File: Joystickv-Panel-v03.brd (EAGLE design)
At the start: 100 x 48.9 mm, 58 parts, among them J1 AVR_SPI_PRG_6PTH, U1 JOYSTICKPTH, U3 V_REG_MIC5219SMD, U4 MCP73831

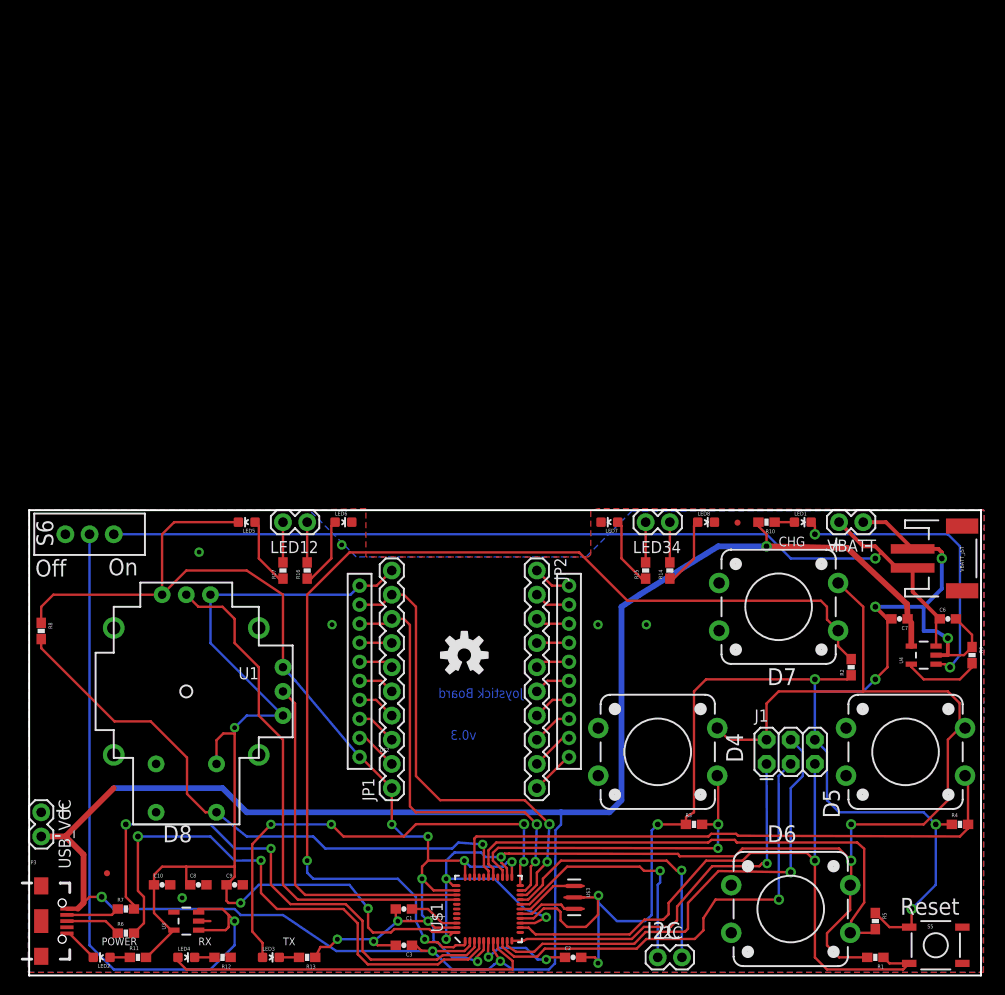
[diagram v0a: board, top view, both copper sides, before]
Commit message: Panel
Finished design, Panelized, and CAMed
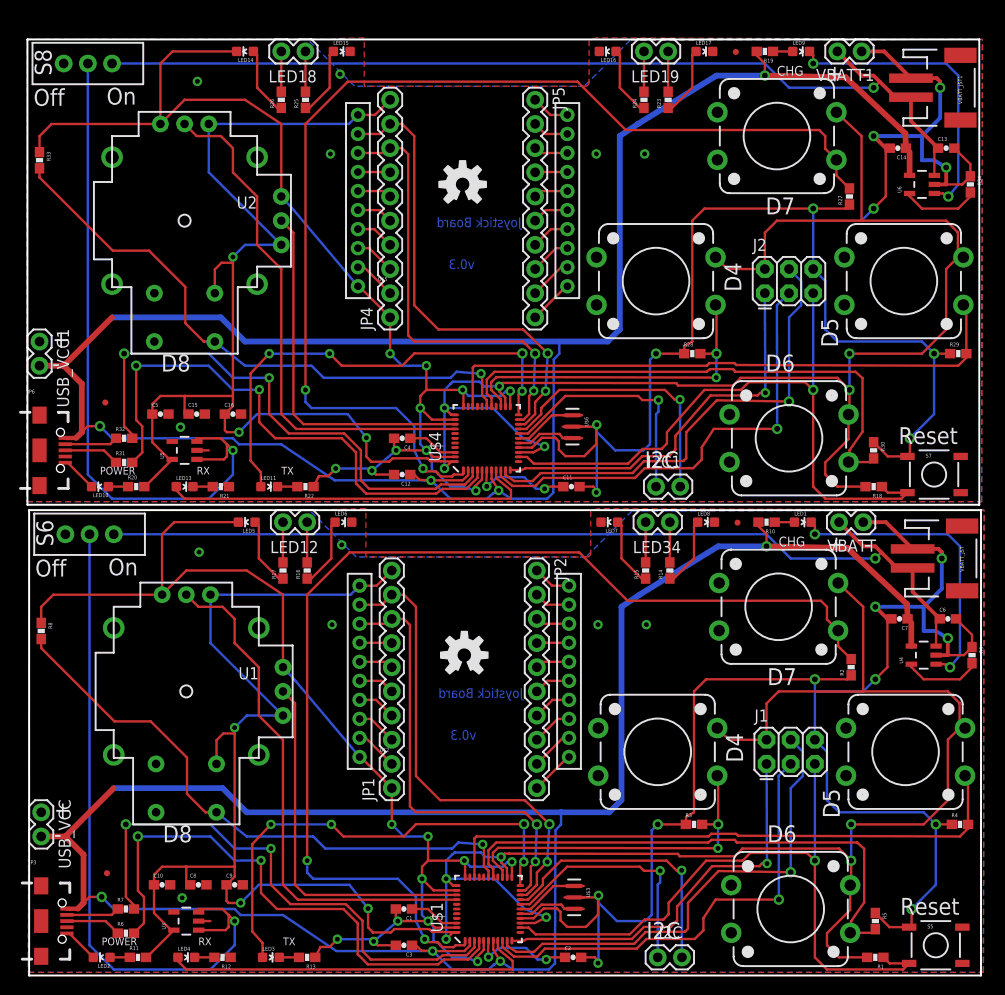
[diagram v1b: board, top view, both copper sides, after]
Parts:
- added C11, C12, C16: 1.0uF, SparkFun-Capacitors:0603-CAP
- added C13, C15: 10uF, SparkFun-Capacitors:0603-CAP
- added C14: 4.7uF, SparkFun-Capacitors:0603-CAP
- added C4, C5: 0.1uF, SparkFun-Capacitors:0603-CAP
- added FID3, FID4: FIDUCIALUFIDUCIAL, SparkFun-Aesthetics:MICRO-FIDUCIAL
- added I2C1, LED18, LED19, USB_VCC1, VBATT1: (no value), SparkFun-Connectors:1X02
- added J2: AVR_SPI_PRG_6PTH, SparkFun-Connectors:2X3
- added JP4, JP5: M10", SparkFun-Connectors:1X10
- added JP6: USB_MICROB_PLUGCONN-11752, SparkFun-Connectors:USB-B-MICRO-SMD_V03
- added LED10, LED16: RED, SparkFun-LED:LED-0603
- added LED11: Green, SparkFun-LED:LED-0603
- added LED13, LED15, LED9: Yellow, SparkFun-LED:LED-0603
- added LED14: GREEN, SparkFun-LED:LED-0603
- added LED17: BLUE, SparkFun-LED:LED-0603
- added LOGO2: OSHW-LOGOM, SparkFun-Aesthetics:OSHW-LOGO-M
- added R18, R27, R28, R29, R30, R33: 10K, SparkFun-Resistors:0603-RES
- added R19, R20: 470, SparkFun-Resistors:0603-RES
- added R21, R22, R23, R24, R25, R26: 330, SparkFun-Resistors:0603-RES
- added R31, R32: 22, SparkFun-Resistors:0603-RES
- added R34: 2.0k, SparkFun-Resistors:0603-RES
- added S10, S11, S12, S9: SWITCH-MOMENTARY-212MM, SparkFun-Electromechanical:TACTILE-PTH-12MM
- added S7: Reset, SparkFun-Electromechanical:TACTILE-SWITCH-SMD
- added S8: (no value), SparkFun-Electromechanical:SWITCH-SPDT
- added U$4: ATMEGA32U41:1-LESS_PASTE, SparkFun-DigitalIC:QFN-44-NOPAD_1:1-LESS_PASTE
- added U$5: XBEE-1B1, SparkFun-RF:XBEE-1
- added U$6: 8MHZ, SparkFun-FreqCtrl:RESONATOR-SMD
- added U2: JOYSTICKPTH, SparkFun-Electromechanical:JOYSTICK
- added U5: V_REG_MIC5219SMD, SparkFun-PowerIC:SOT23-5
- added U6: MCP73831, SparkFun-PowerIC:SOT23-5
- added VBATT_JST1: (no value), SparkFun-Connectors:JST-2-SMD
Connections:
- new net 3.3V1: C15.1, C16.1, C5.1, J2.2, JP4.10, R18.2, R20.2, S10.3, S11.3, S12.3, S9.3, U$4.14, U$4.24, U$4.34, U$4.44, U$5.1, U2.B2A, U2.H1, U2.V1, U5.5
- new net A2: U$4.36, U2.V2
- new net A3: U$4.37, U2.H2
- new net D+1: R31.2, U$4.4
- new net D-1: R32.2, U$4.3
- new net D1: I2C1.2, U$4.18
- new net D11: R28.2, S10.1, U$4.25
- new net D12: R29.2, S11.1, U$4.31
- new net D13: R30.2, S12.1, U$4.27
- new net D14: I2C1.1, U$4.19
- new net D15: R27.2, S9.1, U$4.1
- new net D16: R33.2, U$4.28, U2.B1A
- new net D17: U$4.29
- new net D18: U$4.30
- new net GND1: C11.2, C12.2, C13.2, C14.2, C15.2, C16.2, C4.2, C5.2, J2.6, JP4.1, JP6.GND1, LED10.C, LED14.C, LED15.C, LED16.C, LED17.C, R21.1, R22.1, R27.1, R28.1, R29.1, R30.1, R33.1, R34.1, S7.1, U$4.15, U$4.23, U$4.33, U$4.35, U$4.43, U$4.5, U$5.10, U$6.2, U2.H3, U2.V3, U5.2, U6.2, USB_VCC1.1, VBATT1.1, VBATT_JST1.1
- new net MISO1: J2.1, U$4.11
- new net MOSI1: J2.4, U$4.10
- new net N$22: C11.1, U$4.6
- new net N$41: R34.2, U6.5
- new net N$42: JP4.2, U$5.9
- new net N$43: JP4.3, U$5.8
- new net N$44: JP4.4, U$5.7
- new net N$45: JP4.5, U$5.6
- new net N$46: JP4.6, U$5.5
- new net N$47: JP4.7, U$5.4
- new net N$48: JP5.10, U$5.11
- new net N$49: JP5.9, U$5.12
- new net N$50: JP5.8, U$5.13
- new net N$51: JP5.7, U$5.14
- new net N$52: JP5.6, U$5.15
- new net N$53: JP5.5, U$5.16
- new net N$54: JP5.4, U$5.17
- new net N$55: JP5.3, U$5.18
- new net N$56: JP5.2, U$5.19
- new net N$57: JP5.1, U$5.20
- new net N$58: LED9.A, R19.1
- new net N$59: LED9.C, U6.1
- new net N$60: LED10.A, R20.1
- new net N$61: LED13.A, U$4.8
- new net N$62: LED13.C, R21.2
- new net N$63: LED11.C, R22.2
- new net N$64: LED11.A, U$4.22
- new net N$65: LED15.A, R25.1
- new net N$66: LED14.A, R26.1
- new net N$67: LED18.1, R26.2
- new net N$68: LED18.2, R25.2
- new net N$69: LED19.1, R24.2
- new net N$7: C4.1, U$4.42
- new net N$70: LED19.2, R23.2
- new net N$71: LED17.A, R23.1
- new net N$72: LED16.A, R24.1
- new net N$73: JP6.D+1, R31.1
- new net N$74: JP6.D-1, R32.1
- new net N$75: U$4.17, U$6.1
- new net N$76: U$4.16, U$6.3
- new net RESET1: J2.5, R18.1, S7.3, U$4.13
- new net RX1: JP4.9, U$4.20, U$5.2
- new net SCK1: J2.3, U$4.9
- new net TX1: JP4.8, U$4.21, U$5.3
- new net USB_VCC1: C12.1, C14.1, JP6.VBUS1, R19.2, U$4.2, U$4.7, U6.4, USB_VCC1.2
- new net VBATT1: C13.1, S8.3, U6.3, VBATT1.2, VBATT_JST1.2
- new net VIN1: S8.2, U5.1, U5.3
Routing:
- net GND1: track 0.00 -> 309.7 mm, vias 0 -> 26
- net 3.3V1: track 0.00 -> 272.6 mm, vias 0 -> 9
- net USB_VCC1: track 0.00 -> 215.2 mm, vias 0 -> 4
- net D15: track 0.00 -> 116.8 mm, vias 0 -> 2
- net VBATT1: track 0.00 -> 101.2 mm, vias 0 -> 1
- net VIN1: track 0.00 -> 72.3 mm, vias 0 -> 1
- net RESET1: track 0.00 -> 70.0 mm, vias 0 -> 1
- net D12: track 0.00 -> 62.2 mm
- net D16: track 0.00 -> 62.1 mm, vias 0 -> 1
- net D+1: track 0.00 -> 57.7 mm, vias 0 -> 2
- net D-1: track 0.00 -> 57.0 mm, vias 0 -> 2
- net D13: track 0.00 -> 55.5 mm
- net A3: track 0.00 -> 55.1 mm
- net MOSI1: track 0.00 -> 50.6 mm, vias 0 -> 1
- net RX1: track 0.00 -> 49.8 mm, vias 0 -> 2
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- added copper zone on layer 1, net GND1
- added copper zone on layer 16, net GND1
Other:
- board size 100 x 48.9 mm -> 100.2 x 98.3 mm

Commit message: OSH Panel
OSH requires 100mil between boards to panelize.
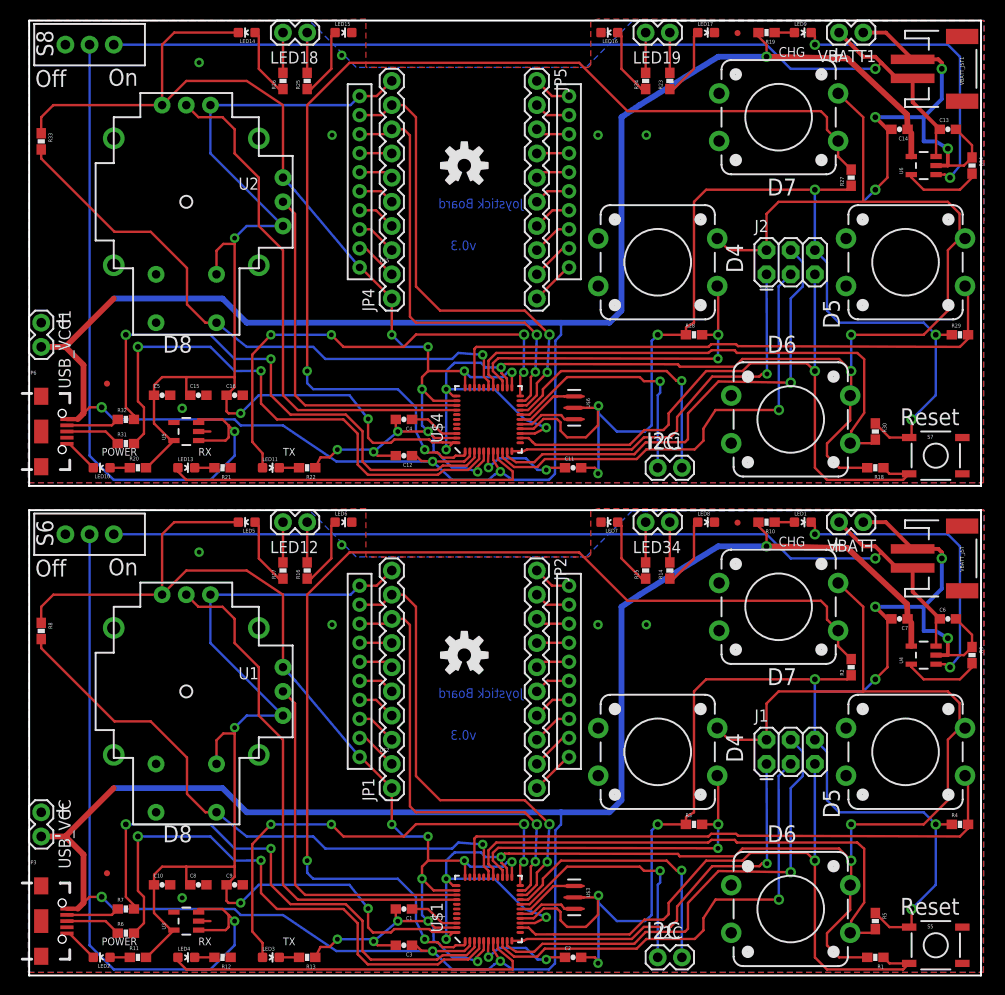
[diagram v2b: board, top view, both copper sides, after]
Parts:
- moved I2C1 1.99 mm to (68.5, 53.3)
- moved J2 1.99 mm to (77.4, 73.6)
- moved JP4 1.99 mm to (38.0, 71.1)
- moved JP5 1.99 mm to (53.3, 94.0)
- moved LED15 1.99 mm to (32.9, 99.0)
- moved LED17 1.99 mm to (71.0, 99.0)
- moved LED9 1.99 mm to (81.2, 99.0)
- moved R18 1.99 mm to (88.8, 53.3)
- moved R19 1.99 mm to (77.4, 99.0)
- moved R23 1.99 mm to (67.2, 94.0)
- moved R27 1.99 mm to (86.3, 83.8)
- moved R29 1.99 mm to (97.7, 67.3)
- moved R30 1.99 mm to (88.8, 57.1)
- moved R34 1.99 mm to (99.0, 85.1)
- moved S10 1.99 mm to (66.0, 74.9)
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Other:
- board size 100.2 x 98.3 mm -> 100 x 100.3 mm
